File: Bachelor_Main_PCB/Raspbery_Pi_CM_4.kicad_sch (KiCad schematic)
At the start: 11 parts, among them J21 M20-9990245, Q12 NX3008NBKW, Q2 SSM3J358R,LF, U1 SC0683, X1 DF40HC_3.0_-100DS-0.4V_58, X2 DF40HC_3.0_-100DS-0.4V_58

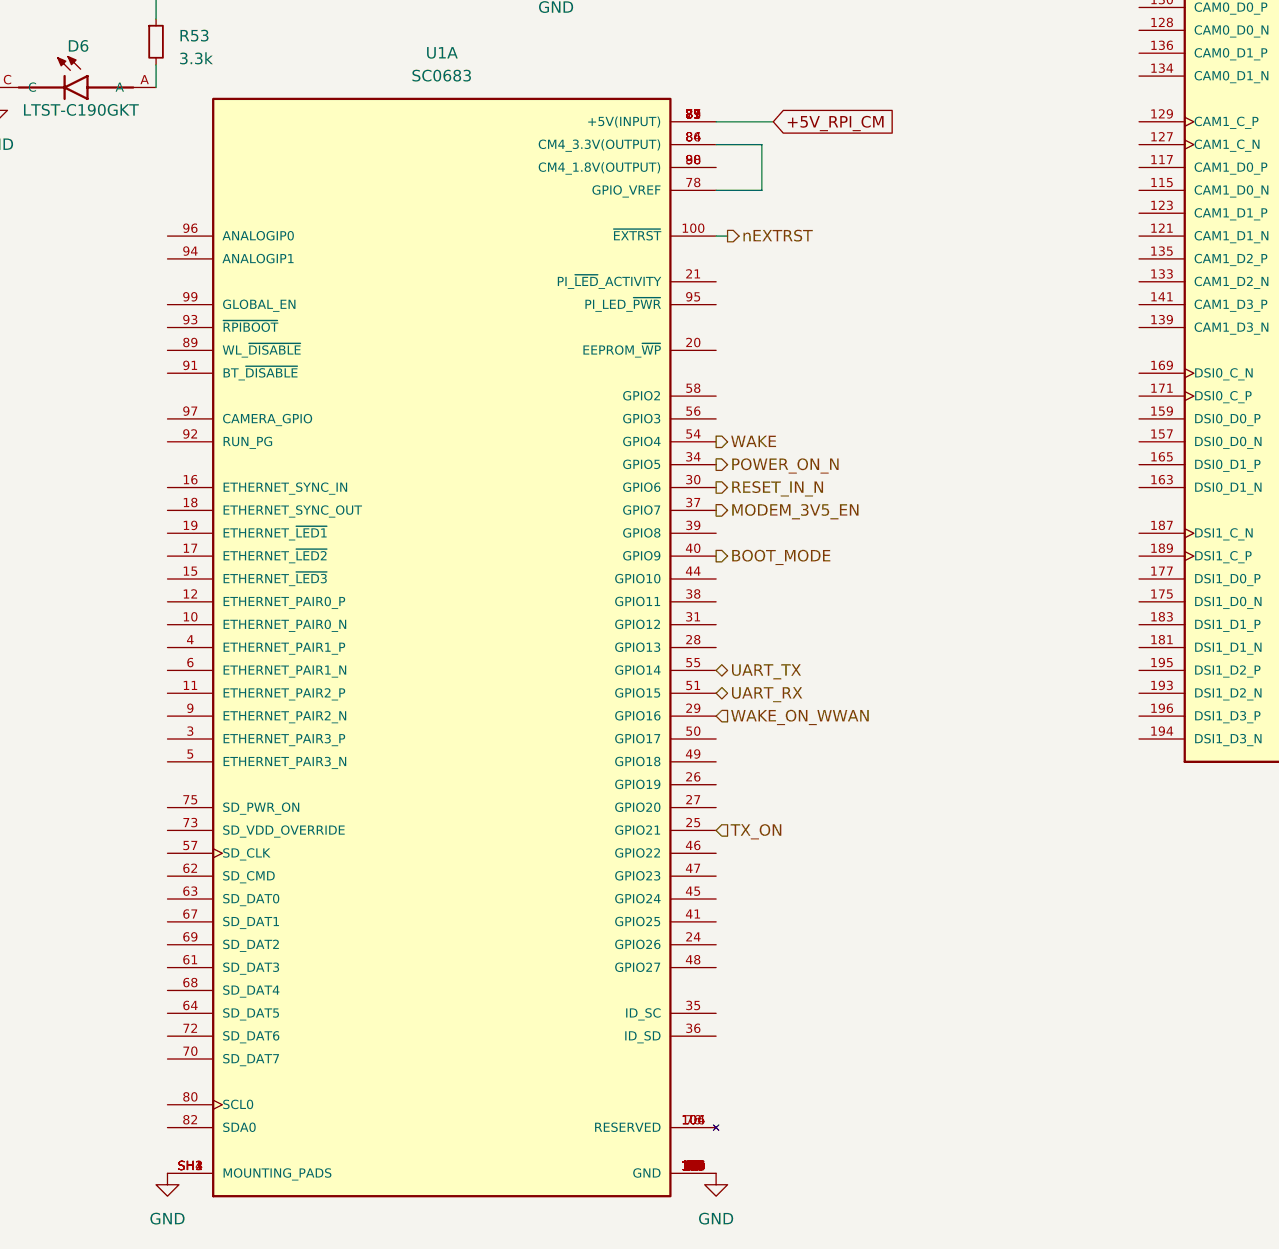
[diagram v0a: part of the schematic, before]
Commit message: Add RPI activity led to pin 21
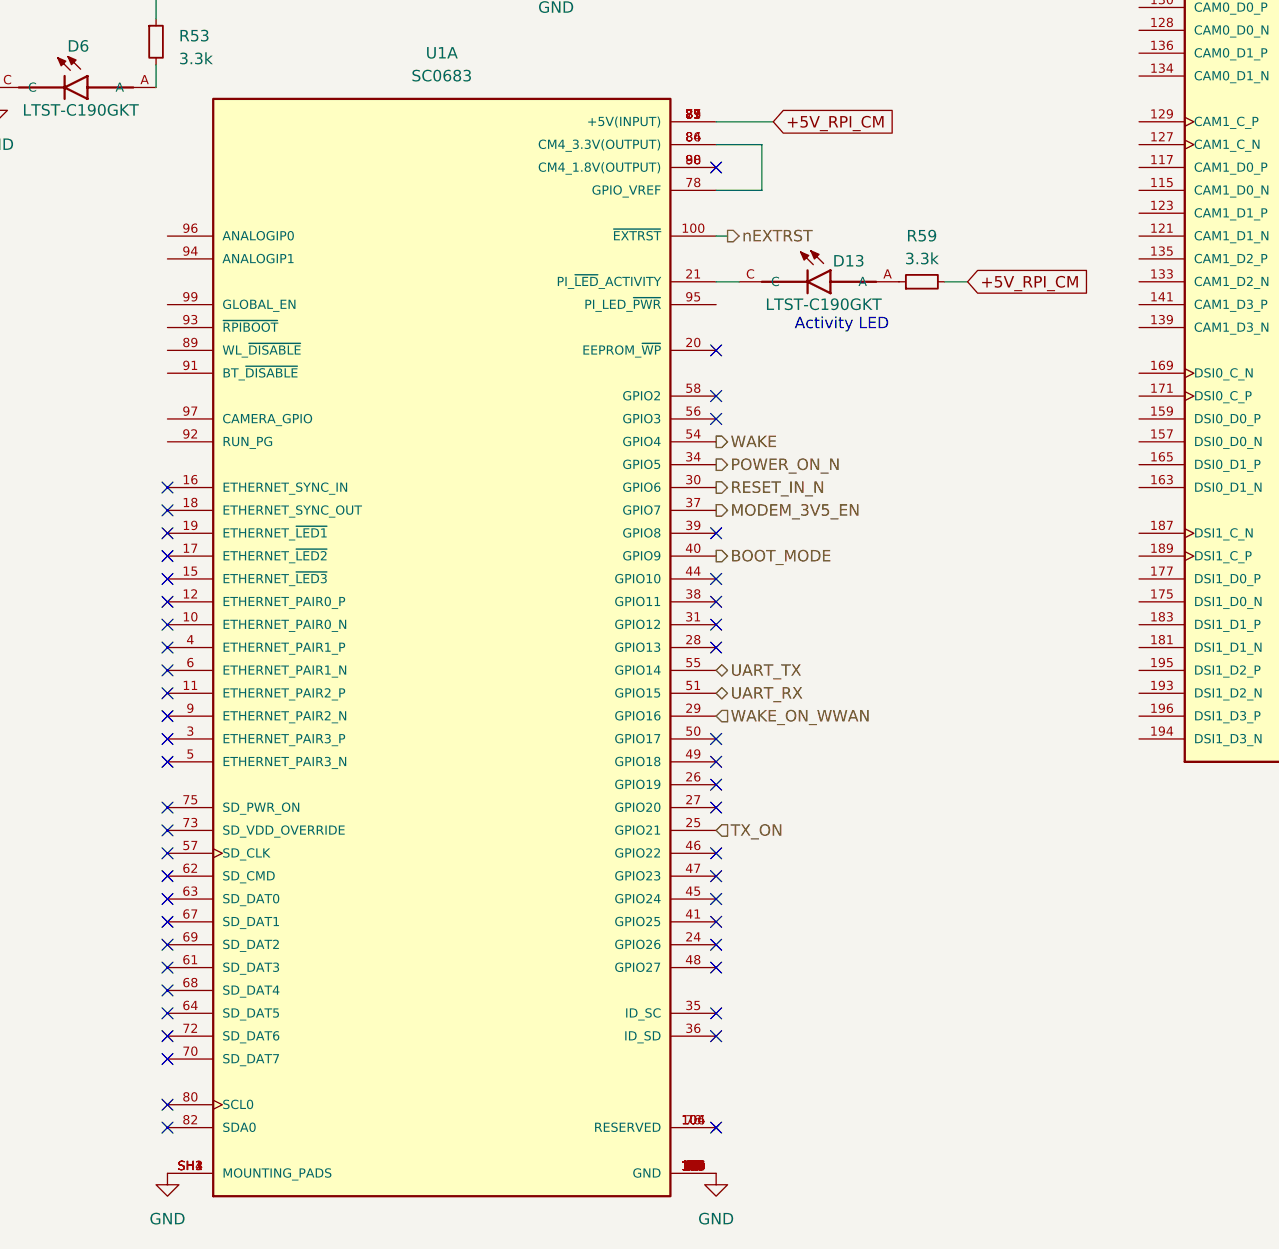
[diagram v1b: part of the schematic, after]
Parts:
- added D13: LTST-C190GKT, LTST-C190GKT:LEDM1608X80, symbol LTST-C190GKT:LTST-C190GKT
- added R59: 3.3k, Resistor_SMD:R_0603_1608Metric, symbol Device:R_Small
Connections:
- net +5V_RPI_CM: now also R59.2
- net at U1.21 (PI_~{LED}_ACTIVITY): now also D13.C
- new net: D13.A, R59.1
- no-connect marks 1 -> 50
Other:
- note added: "Activity LED"

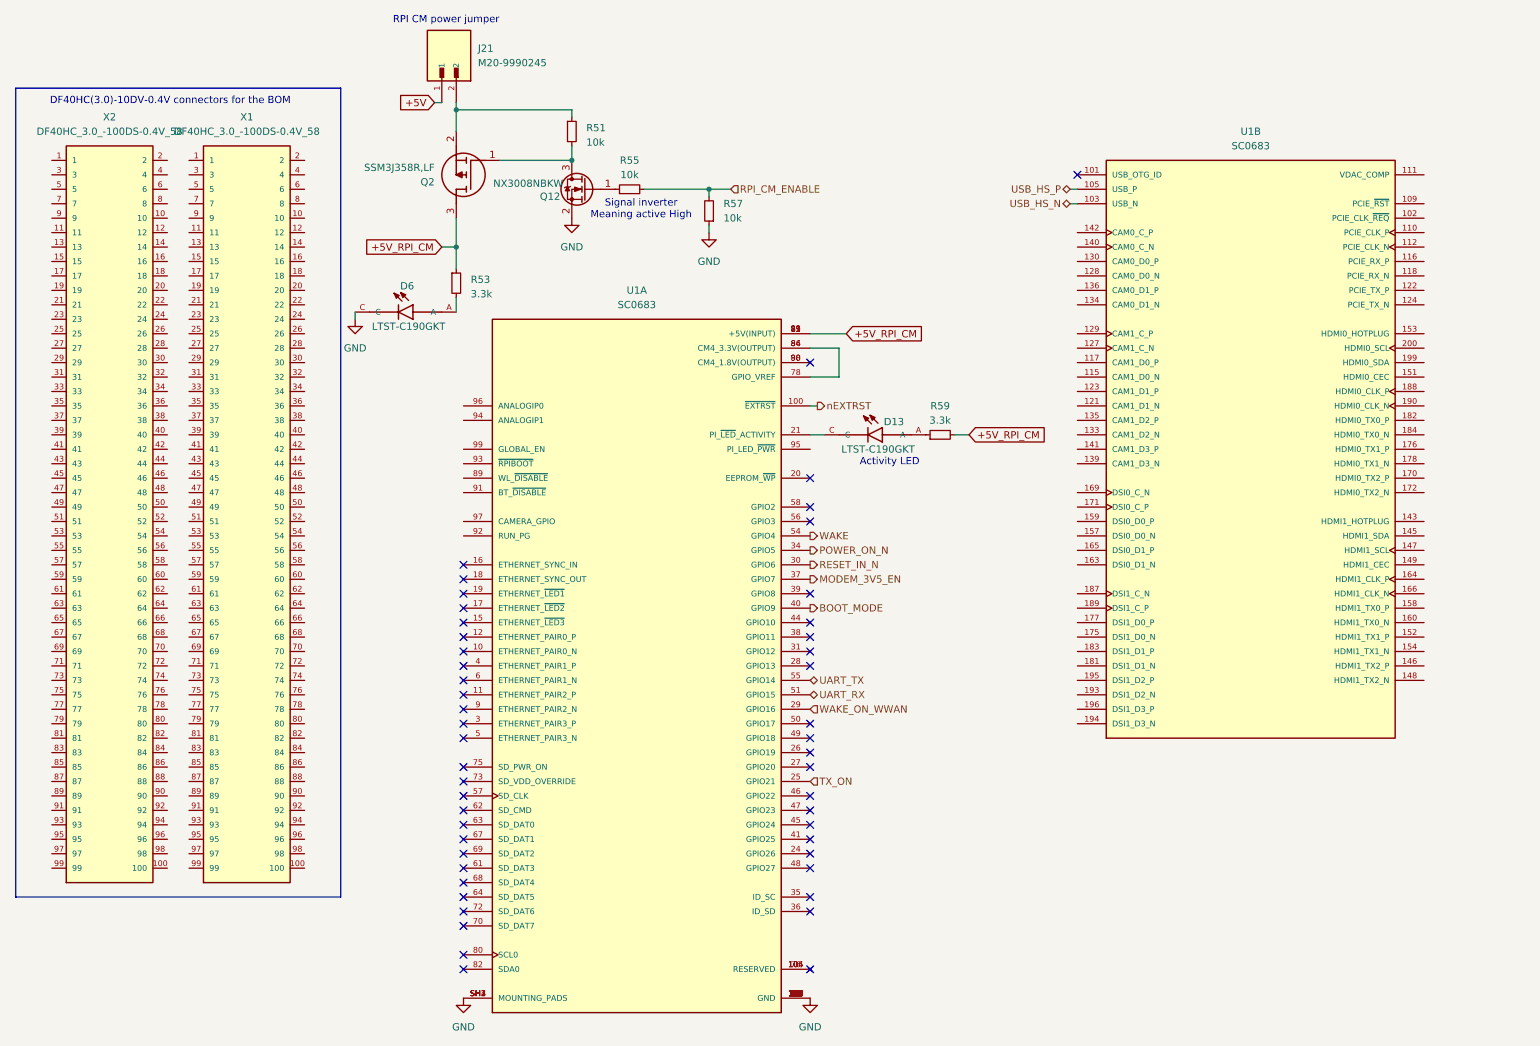
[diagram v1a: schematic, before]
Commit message: Add RPI pins: WL_pins, RUN_PG, RPIBOOT and GLOBAL_EN with a mosfet
the MOSFET to protect against 5v in to MCU
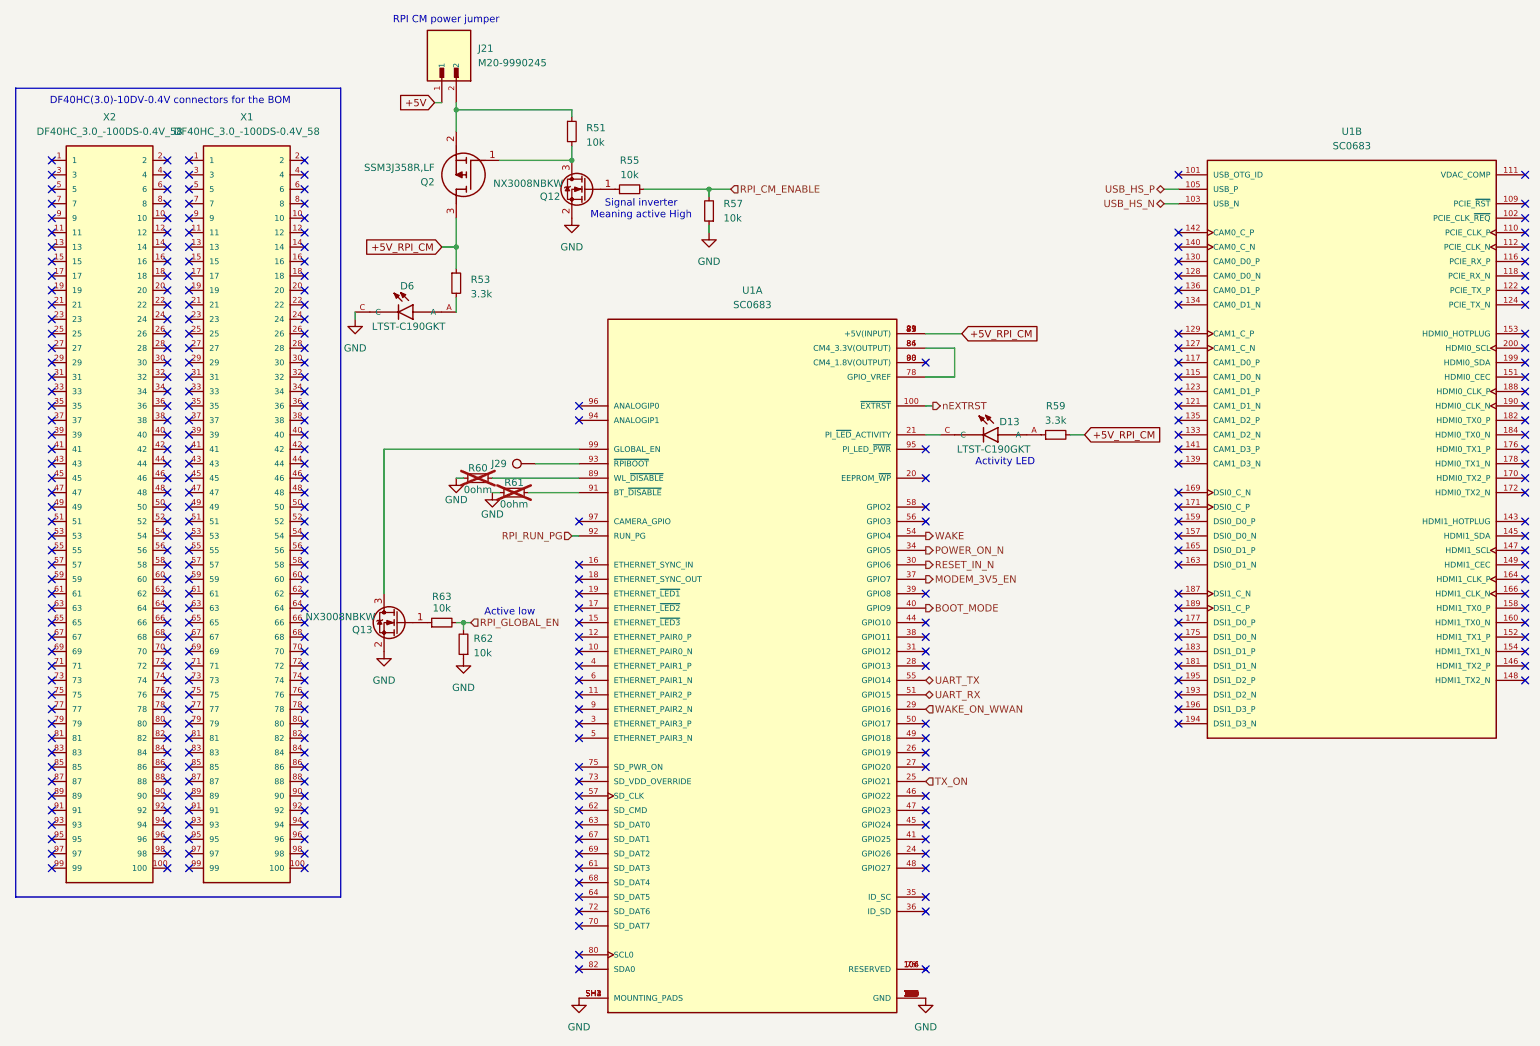
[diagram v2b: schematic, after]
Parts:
- added J29: ~, TestPoint:TestPoint_Pad_D1.0mm, symbol Connector:TestPoint
- added Q13: NX3008NBKW, Package_TO_SOT_SMD:SOT-323_SC-70, symbol Device:Q_NMOS_GSD
- added R60, R61: 0ohm, Resistor_SMD:R_0603_1608Metric, symbol Device:R_Small
- added R62, R63: 10k, Resistor_SMD:R_0603_1608Metric, symbol Device:R_Small
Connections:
- net GND: now also Q13.2 (S), R60.1, R61.1, R62.1
- net at U1.89 (WL_~{DISABLE}): now also R60.2
- net at U1.91 (BT_~{DISABLE}): now also R61.2
- net RPI_RUN_PG: now reaches U1.92 (RUN_PG)
- net at U1.93 (~{RPIBOOT}): now also J29.1
- net at U1.99 (GLOBAL_EN): now also Q13.3 (D)
- new net: Q13.1 (G), R63.1
- new net RPI_GLOBAL_EN: R62.2, R63.2
- no-connect marks 50 -> 319
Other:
- note added: "Active low"
- moved on the sheet: D13, R59, U1A, U1B

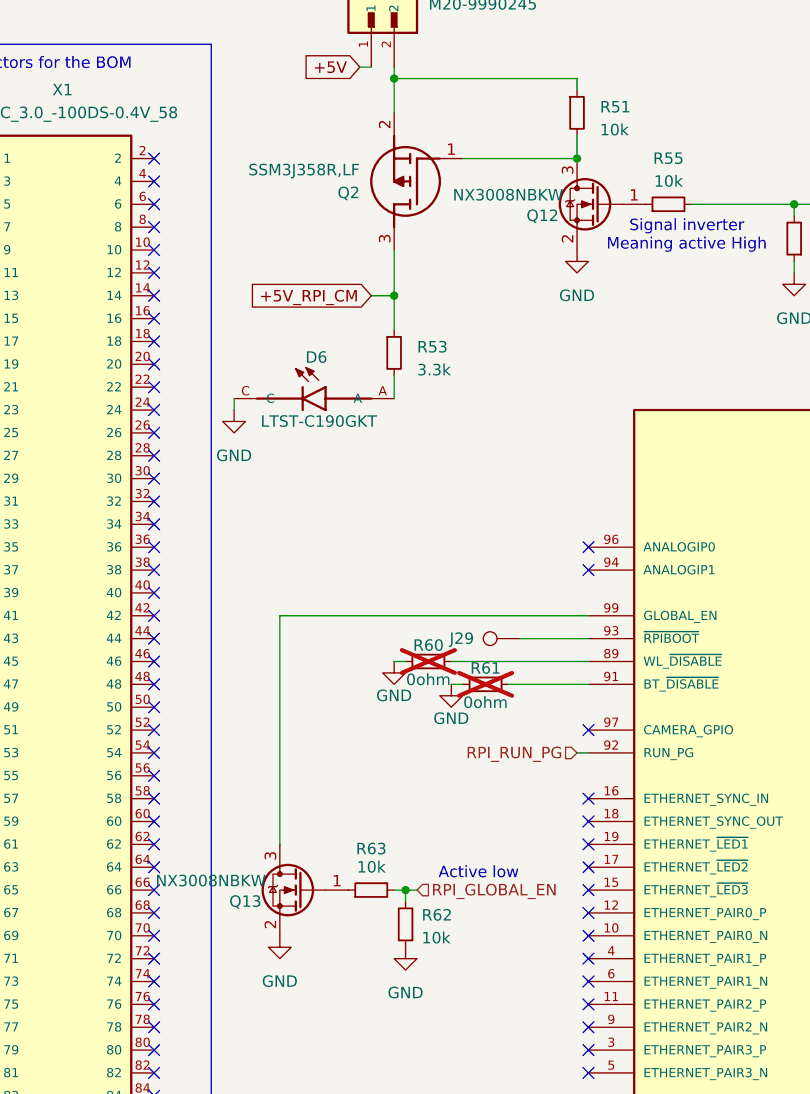
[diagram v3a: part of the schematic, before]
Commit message: Fixed DRC, footprints and power flags and no-connect flags
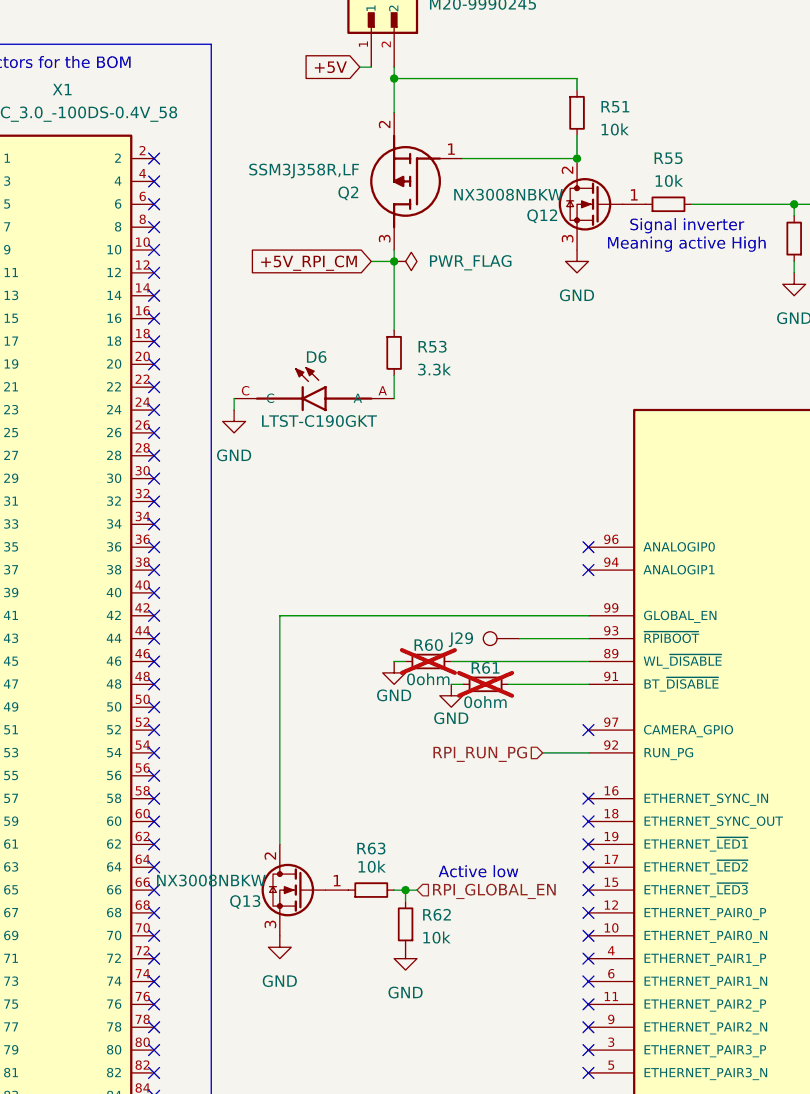
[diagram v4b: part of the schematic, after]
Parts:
- Q12, Q13: symbol Device:Q_NMOS_GSD -> Transistor_FET:Q_NMOS_GDS
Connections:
- net GND: now also Q12.3 (S), Q13.3 (S); no longer Q12.2 (S), Q13.2 (S)
- net at U1.99 (GLOBAL_EN): now also Q13.2 (D); no longer Q13.3 (D)
- net at Q2.1 (G), R51.2: now also Q12.2 (D); no longer Q12.3 (D)

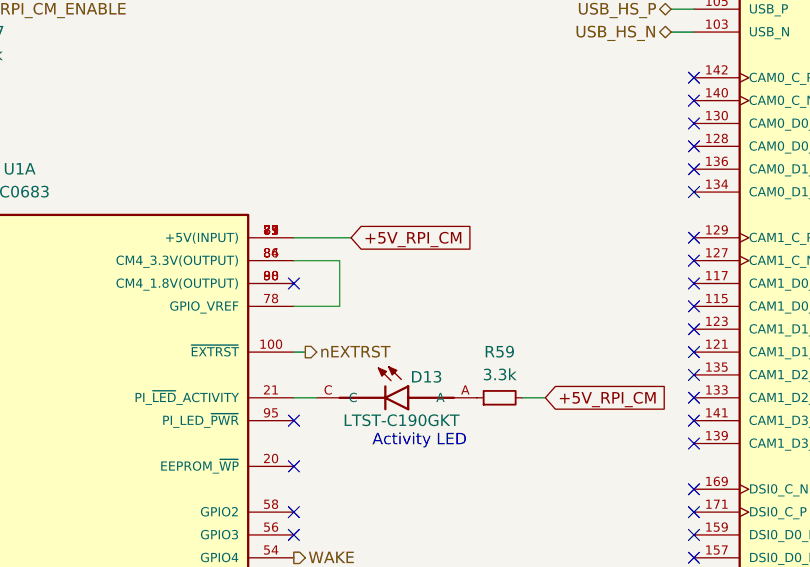
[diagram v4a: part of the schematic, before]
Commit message: Removed Modem_safe_PWR_remove pin.
was potential use for the MCU but would require level shifters and would not add any functionality ass the RPI controls the Modem anyway.
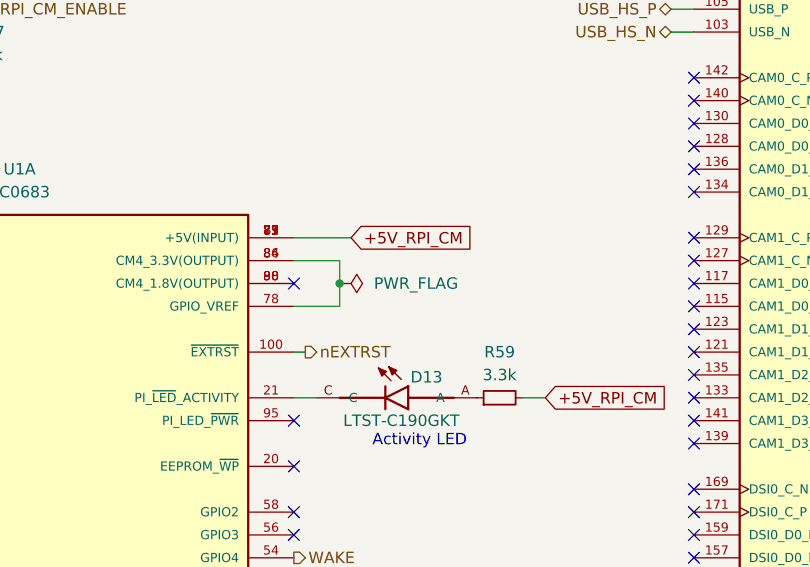
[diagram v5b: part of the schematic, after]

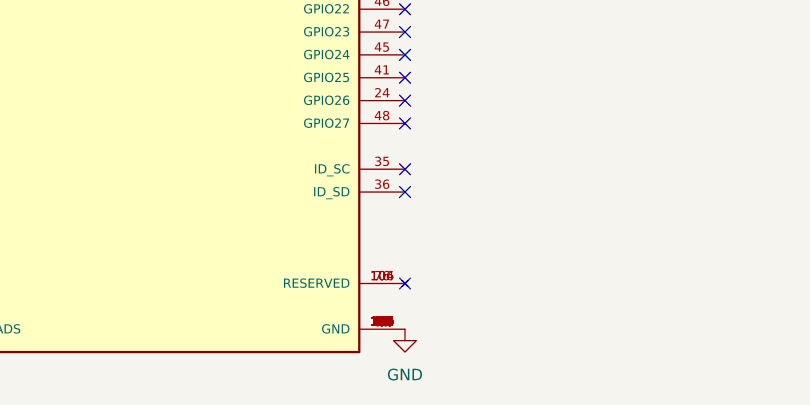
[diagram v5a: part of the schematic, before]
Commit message: Fix all DRC errors and warnings
except not connected pins still unrouted to MCU
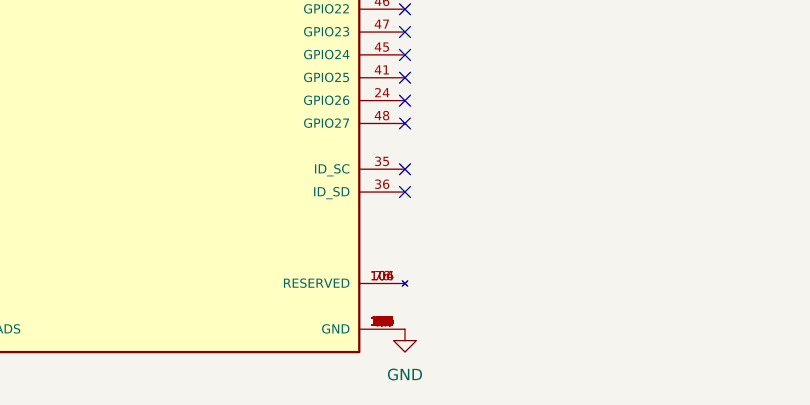
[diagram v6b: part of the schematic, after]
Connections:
- no-connect marks 319 -> 318
